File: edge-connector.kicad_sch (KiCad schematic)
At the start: 5 parts

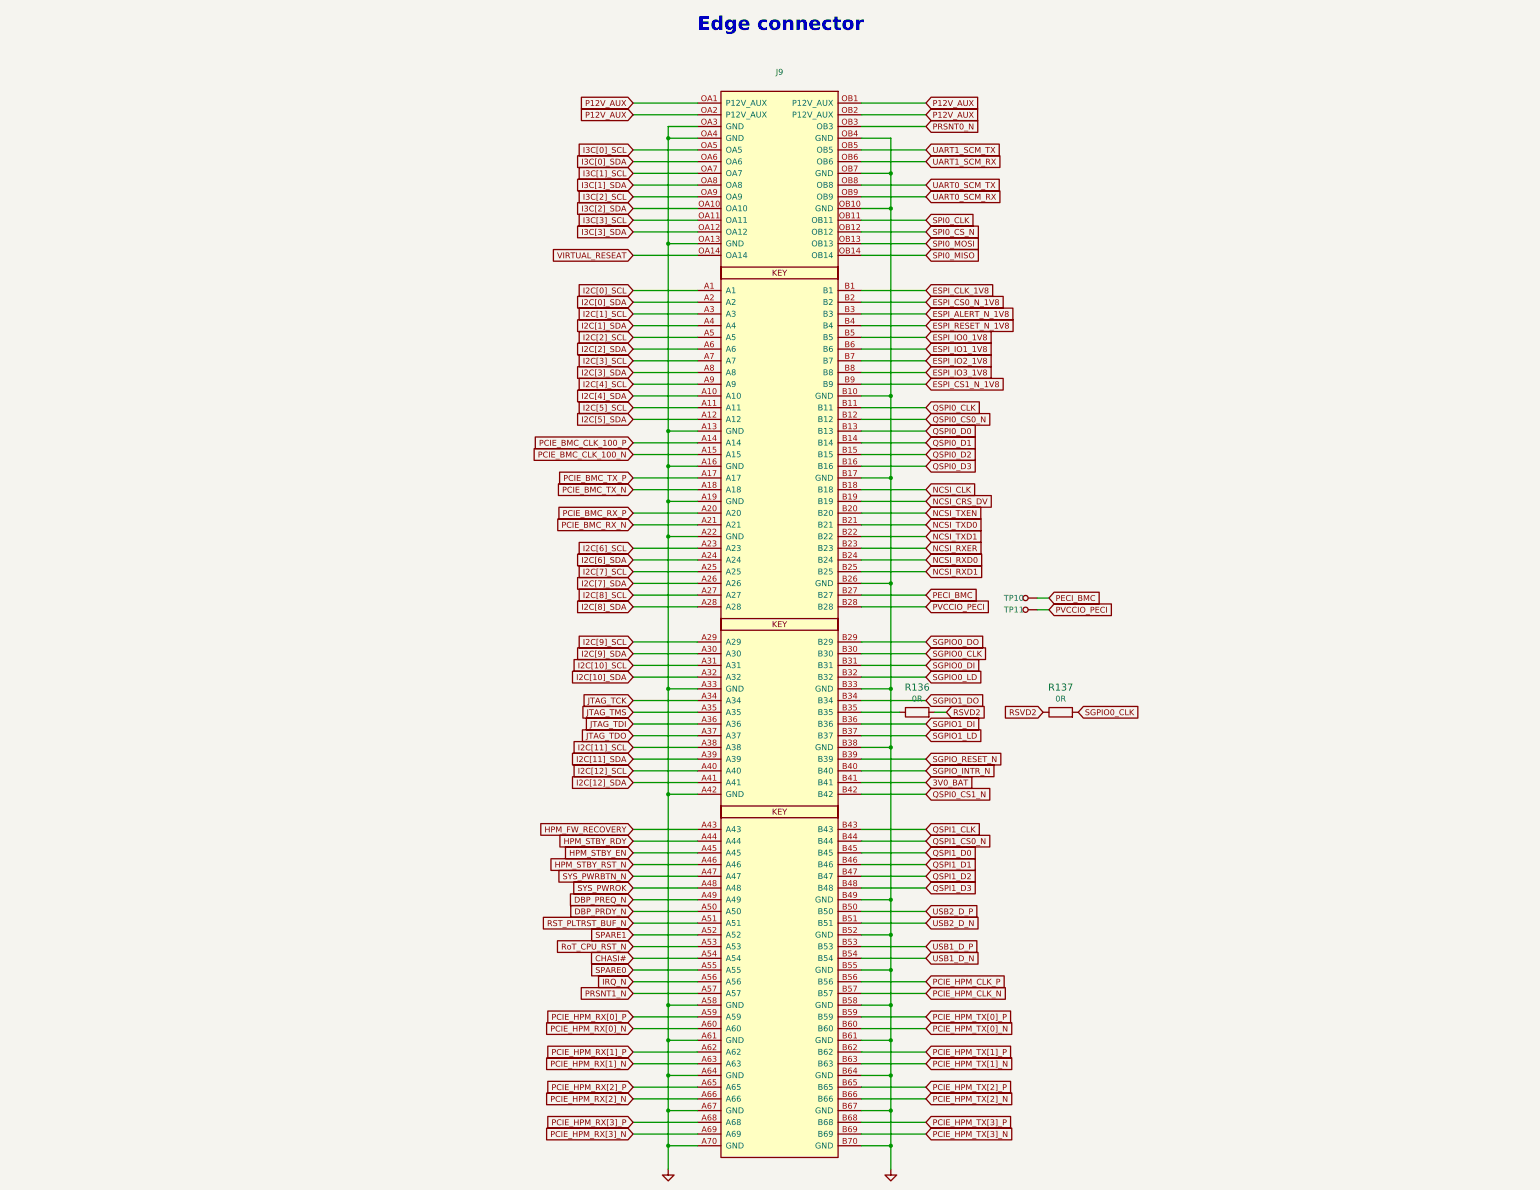
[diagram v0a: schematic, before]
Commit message: Introduce component standardization
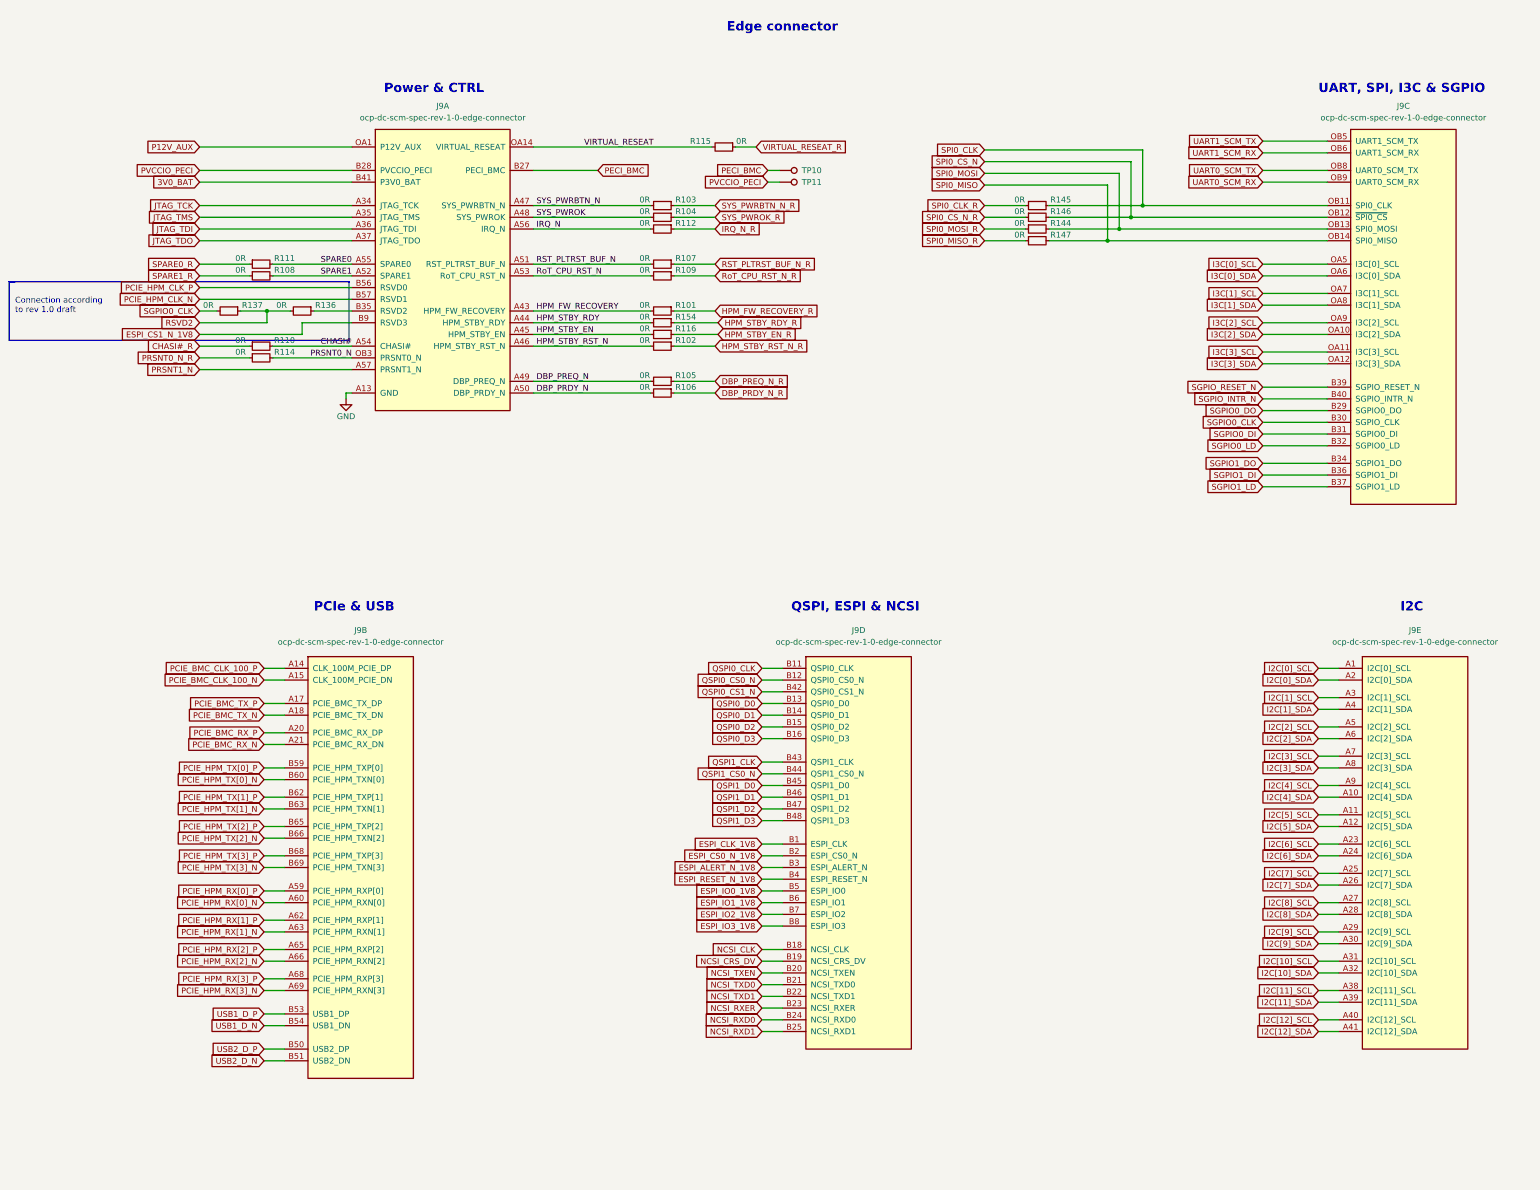
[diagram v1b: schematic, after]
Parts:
- added unit 5 of J9
- added unit 4 of J9
- added unit 2 of J9
- added unit 3 of J9
- added R101, R102, R103, R104, R105, R106, R107, R108, R109, R110, R111, R112, R114, R115, R116, R144, R145, R146, R147, R154: R_0R_0402, antmicro-footprints:R_0402_1005Metric, symbol antmicroResistors0402:R_0R_0402
- J9: value (none) -> ocp-dc-scm-spec-rev-1-0-edge-connector; footprint (none) -> antmicro-footprints:SFF-TA-1002-4C+; symbol artix-dc-scm:SFF-TA-1002-4C+ -> antmicroPciConnectors:ocp-dc-scm-spec-rev-1-0-edge-connector; Author (none) -> Antmicro; License (none) -> Apache-2.0
- R136, R137: value (none) -> R_0R_0402; footprint (none) -> antmicro-footprints:R_0402_1005Metric; symbol artix-dc-scm:R_0R_0402 -> antmicroResistors0402:R_0R_0402; Author (none) -> Antmicro; Current (none) -> 1A; License (none) -> Apache-2.0; Manufacturer PANASONIC -> Panasonic
- TP10, TP11: value (none) -> TP_SMD1MM; footprint (none) -> antmicro-footprints:Testpoint_smd_1mm; symbol artix-dc-scm:TP_SMD1MM -> antmicroTestPoints:TP_1mm_SMD; Author (none) -> Antmicro; DNP (none) -> DNP; License (none) -> Apache-2.0
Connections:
- net CHASI#: now also R110.2
- net DBP_PRDY_N: now also R106.2
- net DBP_PREQ_N: now also R105.2
- net ESPI_ALERT_N_1V8: now also J9.B3 (ESPI_ALERT_N); no longer J9.B3
- net ESPI_CLK_1V8: now also J9.B1 (ESPI_CLK); no longer J9.B1
- net ESPI_CS0_N_1V8: now also J9.B2 (ESPI_CS0_N); no longer J9.B2
- net ESPI_IO0_1V8: now also J9.B5 (ESPI_IO0); no longer J9.B5
- net ESPI_IO1_1V8: now also J9.B6 (ESPI_IO1); no longer J9.B6
- net ESPI_IO2_1V8: now also J9.B7 (ESPI_IO2); no longer J9.B7
- net ESPI_IO3_1V8: now also J9.B8 (ESPI_IO3); no longer J9.B8
- net ESPI_RESET_N_1V8: now also J9.B4 (ESPI_RESET_N); no longer J9.B4
- net HPM_FW_RECOVERY: now also R101.2
- net HPM_STBY_EN: now also R116.2
- net HPM_STBY_RDY: now also R154.2
- net HPM_STBY_RST_N: now also R102.2
- net I2C[0]_SCL: now also J9.A1 (I2C[0]_SCL); no longer J9.A1
- net I2C[0]_SDA: now also J9.A2 (I2C[0]_SDA); no longer J9.A2
- net I2C[10]_SCL: now also J9.A31 (I2C[10]_SCL); no longer J9.A31
- net I2C[10]_SDA: now also J9.A32 (I2C[10]_SDA); no longer J9.A32
- net I2C[11]_SCL: now also J9.A38 (I2C[11]_SCL); no longer J9.A38
- net I2C[11]_SDA: now also J9.A39 (I2C[11]_SDA); no longer J9.A39
- net I2C[12]_SCL: now also J9.A40 (I2C[12]_SCL); no longer J9.A40
- net I2C[12]_SDA: now also J9.A41 (I2C[12]_SDA); no longer J9.A41
- net I2C[1]_SCL: now also J9.A3 (I2C[1]_SCL); no longer J9.A3
- net I2C[1]_SDA: now also J9.A4 (I2C[1]_SDA); no longer J9.A4
- net I2C[2]_SCL: now also J9.A5 (I2C[2]_SCL); no longer J9.A5
- net I2C[2]_SDA: now also J9.A6 (I2C[2]_SDA); no longer J9.A6
- net I2C[3]_SCL: now also J9.A7 (I2C[3]_SCL); no longer J9.A7
- net I2C[3]_SDA: now also J9.A8 (I2C[3]_SDA); no longer J9.A8
- net I2C[4]_SCL: now also J9.A9 (I2C[4]_SCL); no longer J9.A9
- net I2C[4]_SDA: now also J9.A10 (I2C[4]_SDA); no longer J9.A10
- net I2C[5]_SCL: now also J9.A11 (I2C[5]_SCL); no longer J9.A11
- net I2C[5]_SDA: now also J9.A12 (I2C[5]_SDA); no longer J9.A12
- net I2C[6]_SCL: now also J9.A23 (I2C[6]_SCL); no longer J9.A23
- net I2C[6]_SDA: now also J9.A24 (I2C[6]_SDA); no longer J9.A24
- net I2C[7]_SCL: now also J9.A25 (I2C[7]_SCL); no longer J9.A25
- net I2C[7]_SDA: now also J9.A26 (I2C[7]_SDA); no longer J9.A26
- net I2C[8]_SCL: now also J9.A27 (I2C[8]_SCL); no longer J9.A27
- net I2C[8]_SDA: now also J9.A28 (I2C[8]_SDA); no longer J9.A28
- net I2C[9]_SCL: now also J9.A29 (I2C[9]_SCL); no longer J9.A29
- net I2C[9]_SDA: now also J9.A30 (I2C[9]_SDA); no longer J9.A30
- net I3C[0]_SCL: now also J9.OA5 (I3C[0]_SCL); no longer J9.OA5
- net I3C[0]_SDA: now also J9.OA6 (I3C[0]_SDA); no longer J9.OA6
- net I3C[1]_SCL: now also J9.OA7 (I3C[1]_SCL); no longer J9.OA7
- net I3C[1]_SDA: now also J9.OA8 (I3C[1]_SDA); no longer J9.OA8
- net I3C[2]_SCL: now also J9.OA9 (I3C[2]_SCL); no longer J9.OA9
- net I3C[2]_SDA: now also J9.OA10 (I3C[2]_SDA); no longer J9.OA10
- net I3C[3]_SCL: now also J9.OA11 (I3C[3]_SCL); no longer J9.OA11
- net I3C[3]_SDA: now also J9.OA12 (I3C[3]_SDA); no longer J9.OA12
- net IRQ_N: now also R112.2
- net NCSI_CLK: now also J9.B18 (NCSI_CLK); no longer J9.B18
- net NCSI_CRS_DV: now also J9.B19 (NCSI_CRS_DV); no longer J9.B19
- net NCSI_RXD0: now also J9.B24 (NCSI_RXD0); no longer J9.B24
- net NCSI_RXD1: now also J9.B25 (NCSI_RXD1); no longer J9.B25
- net NCSI_RXER: now also J9.B23 (NCSI_RXER); no longer J9.B23
- net NCSI_TXD0: now also J9.B21 (NCSI_TXD0); no longer J9.B21
- net NCSI_TXD1: now also J9.B22 (NCSI_TXD1); no longer J9.B22
- net NCSI_TXEN: now also J9.B20 (NCSI_TXEN); no longer J9.B20
- net PCIE_BMC_CLK_100_N: now also J9.A15 (CLK_100M_PCIE_DN); no longer J9.A15
- net PCIE_BMC_CLK_100_P: now also J9.A14 (CLK_100M_PCIE_DP); no longer J9.A14
- net PCIE_BMC_RX_N: now also J9.A21 (PCIE_BMC_RX_DN); no longer J9.A21
- net PCIE_BMC_RX_P: now also J9.A20 (PCIE_BMC_RX_DP); no longer J9.A20
- net PCIE_BMC_TX_N: now also J9.A18 (PCIE_BMC_TX_DN); no longer J9.A18
- net PCIE_BMC_TX_P: now also J9.A17 (PCIE_BMC_TX_DP); no longer J9.A17
- net PCIE_HPM_RX[0]_N: now also J9.A60 (PCIE_HPM_RXN[0]); no longer J9.A60
- net PCIE_HPM_RX[0]_P: now also J9.A59 (PCIE_HPM_RXP[0]); no longer J9.A59
- net PCIE_HPM_RX[1]_N: now also J9.A63 (PCIE_HPM_RXN[1]); no longer J9.A63
- net PCIE_HPM_RX[1]_P: now also J9.A62 (PCIE_HPM_RXP[1]); no longer J9.A62
- net PCIE_HPM_RX[2]_N: now also J9.A66 (PCIE_HPM_RXN[2]); no longer J9.A66
- net PCIE_HPM_RX[2]_P: now also J9.A65 (PCIE_HPM_RXP[2]); no longer J9.A65
- net PCIE_HPM_RX[3]_N: now also J9.A69 (PCIE_HPM_RXN[3]); no longer J9.A69
- net PCIE_HPM_RX[3]_P: now also J9.A68 (PCIE_HPM_RXP[3]); no longer J9.A68
- net PCIE_HPM_TX[0]_N: now also J9.B60 (PCIE_HPM_TXN[0]); no longer J9.B60
- net PCIE_HPM_TX[0]_P: now also J9.B59 (PCIE_HPM_TXP[0]); no longer J9.B59
- net PCIE_HPM_TX[1]_N: now also J9.B63 (PCIE_HPM_TXN[1]); no longer J9.B63
- net PCIE_HPM_TX[1]_P: now also J9.B62 (PCIE_HPM_TXP[1]); no longer J9.B62
- net PCIE_HPM_TX[2]_N: now also J9.B66 (PCIE_HPM_TXN[2]); no longer J9.B66
- net PCIE_HPM_TX[2]_P: now also J9.B65 (PCIE_HPM_TXP[2]); no longer J9.B65
- net PCIE_HPM_TX[3]_N: now also J9.B69 (PCIE_HPM_TXN[3]); no longer J9.B69
- net PCIE_HPM_TX[3]_P: now also J9.B68 (PCIE_HPM_TXP[3]); no longer J9.B68
- net PRSNT0_N: now also R114.2
- net QSPI0_CLK: now also J9.B11 (QSPI0_CLK); no longer J9.B11
- net QSPI0_CS0_N: now also J9.B12 (QSPI0_CS0_N); no longer J9.B12
- net QSPI0_CS1_N: now also J9.B42 (QSPI0_CS1_N); no longer J9.B42
- net QSPI0_D0: now also J9.B13 (QSPI0_D0); no longer J9.B13
- net QSPI0_D1: now also J9.B14 (QSPI0_D1); no longer J9.B14
- net QSPI0_D2: now also J9.B15 (QSPI0_D2); no longer J9.B15
- net QSPI0_D3: now also J9.B16 (QSPI0_D3); no longer J9.B16
- net QSPI1_CLK: now also J9.B43 (QSPI1_CLK); no longer J9.B43
- net QSPI1_CS0_N: now also J9.B44 (QSPI1_CS0_N); no longer J9.B44
- net QSPI1_D0: now also J9.B45 (QSPI1_D0); no longer J9.B45
- net QSPI1_D1: now also J9.B46 (QSPI1_D1); no longer J9.B46
- net QSPI1_D2: now also J9.B47 (QSPI1_D2); no longer J9.B47
- net QSPI1_D3: now also J9.B48 (QSPI1_D3); no longer J9.B48
- net RST_PLTRST_BUF_N: now also R107.2
- net RoT_CPU_RST_N: now also R109.2
- net SGPIO0_CLK: now also J9.B30 (SGPIO_CLK); no longer J9.B30
- net SGPIO0_DI: now also J9.B31 (SGPIO0_DI); no longer J9.B31
- net SGPIO0_DO: now also J9.B29 (SGPIO0_DO); no longer J9.B29
- net SGPIO0_LD: now also J9.B32 (SGPIO0_LD); no longer J9.B32
- net SGPIO1_DI: now also J9.B36 (SGPIO1_DI); no longer J9.B36
- net SGPIO1_DO: now also J9.B34 (SGPIO1_DO); no longer J9.B34
- net SGPIO1_LD: now also J9.B37 (SGPIO1_LD); no longer J9.B37
- net SGPIO_INTR_N: now also J9.B40 (SGPIO_INTR_N); no longer J9.B40
- net SGPIO_RESET_N: now also J9.B39 (SGPIO_RESET_N); no longer J9.B39
- net SPARE0: now also R111.2
- net SPARE1: now also R108.2
- net SPI0_CLK: now also J9.OB11 (SPI0_CLK), R145.2; no longer J9.OB11
- net SPI0_CS_N: now also J9.OB12 (~{SPI0_CS}), R146.2; no longer J9.OB12
- net SPI0_MISO: now also J9.OB14 (SPI0_MISO), R147.2; no longer J9.OB14
- net SPI0_MOSI: now also J9.OB13 (SPI0_MOSI), R144.2; no longer J9.OB13
- net SYS_PWRBTN_N: now also R103.2
- net SYS_PWROK: now also R104.2
- net UART0_SCM_RX: now also J9.OB9 (UART0_SCM_RX); no longer J9.OB9
- net UART0_SCM_TX: now also J9.OB8 (UART0_SCM_TX); no longer J9.OB8
- net UART1_SCM_RX: now also J9.OB6 (UART1_SCM_RX); no longer J9.OB6
- net UART1_SCM_TX: now also J9.OB5 (UART1_SCM_TX); no longer J9.OB5
- net USB1_D_N: now also J9.B54 (USB1_DN); no longer J9.B54
- net USB1_D_P: now also J9.B53 (USB1_DP); no longer J9.B53
- net USB2_D_N: now also J9.B51 (USB2_DN); no longer J9.B51
- net USB2_D_P: now also J9.B50 (USB2_DP); no longer J9.B50
- net VIRTUAL_RESEAT: now also R115.2
- new net CHASI#_R: R110.1
- new net DBP_PRDY_N_R: R106.1
- new net DBP_PREQ_N_R: R105.1
- new net HPM_FW_RECOVERY_R: R101.1
- new net HPM_STBY_EN_R: R116.1
- new net HPM_STBY_RDY_R: R154.1
- new net HPM_STBY_RST_N_R: R102.1
- new net IRQ_N_R: R112.1
- new net PRSNT0_N_R: R114.1
- new net RST_PLTRST_BUF_N_R: R107.1
- new net RoT_CPU_RST_N_R: R109.1
- new net SPARE0_R: R111.1
- new net SPARE1_R: R108.1
- new net SPI0_CLK_R: R145.1
- new net SPI0_CS_N_R: R146.1
- new net SPI0_MISO_R: R147.1
- new net SPI0_MOSI_R: R144.1
- new net SYS_PWRBTN_N_R: R103.1
- new net SYS_PWROK_R: R104.1
- new net VIRTUAL_RESEAT_R: R115.1
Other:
- note added: "Connection according to rev 1.0 draft"
- note added: "I2C"
- note added: "PCIe & USB"
- note added: "Power & CTRL"
- note added: "QSPI, ESPI & NCSI"
- note added: "UART, SPI, I3C & SGPIO"
- moved on the sheet: R136, R137, TP10, TP11

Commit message: Fix schematic ERC errors. ERC clean
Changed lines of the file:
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@@
     (stroke (width 0) (type default) (color 0 0 0 0))
   )
-  (wire (pts (xy 107.315 48.26) (xy 74.295 48.26))
+  (wire (pts (xy 74.295 48.26) (xy 107.315 48.26))
     (stroke (width 0) (type default) (color 0 0 0 0))
   )
@@
       (effects (font (size 1.27 1.27)) hide)
     )
+    (property "Author" "Antmicro" (id 4) (at 114.935 110.49 0)
+      (effects (font (size 1.27 1.27) (thickness 0.15)) (justify left bottom) hide)
+    )
+    (property "License" "Apache-2.0" (id 5) (at 114.935 113.03 0)
+      (effects (font (size 1.27 1.27) (thickness 0.15)) (justify left bottom) hide)
+    )
     (pin "1")
   )
-  (symbol (lib_id "antmicroPciConnectors:ocp-dc-scm-spec-rev-1-0-edge-connector") (at 321.31 161.29 0) (unit 5)
+  (symbol (lib_name "ocp-dc-scm-spec-rev-1-0-edge-connector_2") (lib_id "antmicroPciConnectors:ocp-dc-scm-spec-rev-1-0-edge-connector") (at 321.31 161.29 0) (unit 5)
     (in_bom yes) (on_board yes) (fields_autoplaced)
     (property "Reference" "J9" (id 0) (at 337.82 153.035 0)
@@
     (pin "A9")
   )
-  (symbol (lib_id "antmicroPciConnectors:ocp-dc-scm-spec-rev-1-0-edge-connector") (at 200.66 161.29 0) (unit 4)
+  (symbol (lib_name "ocp-dc-scm-spec-rev-1-0-edge-connector_3") (lib_id "antmicroPciConnectors:ocp-dc-scm-spec-rev-1-0-edge-connector") (at 200.66 161.29 0) (unit 4)
     (in_bom yes) (on_board yes) (fields_autoplaced)
     (property "Reference" "J9" (id 0) (at 217.17 153.035 0)
@@
     (pin "2")
   )
-  (symbol (lib_id "antmicroPciConnectors:ocp-dc-scm-spec-rev-1-0-edge-connector") (at 92.71 161.29 0) (unit 2)
+  (symbol (lib_name "ocp-dc-scm-spec-rev-1-0-edge-connector_4") (lib_id "antmicroPciConnectors:ocp-dc-scm-spec-rev-1-0-edge-connector") (at 92.71 161.29 0) (unit 2)
     (in_bom yes) (on_board yes) (fields_autoplaced)
     (property "Reference" "J9" (id 0) (at 109.22 153.035 0)
@@
     (pin "2")
   )
-  (symbol (lib_name "ocp-dc-scm-spec-rev-1-0-edge-connector_1") (lib_id "antmicroPciConnectors:ocp-dc-scm-spec-rev-1-0-edge-connector") (at 318.77 46.99 0) (unit 3)
+  (symbol (lib_id "antmicroPciConnectors:ocp-dc-scm-spec-rev-1-0-edge-connector") (at 318.77 46.99 0) (unit 3)
     (in_bom yes) (on_board yes) (fields_autoplaced)
     (property "Reference" "J9" (id 0) (at 335.28 39.37 0)
